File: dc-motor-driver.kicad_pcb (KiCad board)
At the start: 2 copper layers, 33 x 39.5 mm, 29 parts, among them J1 Conn_01x03, J10 Right, J11 RL, J12 RR, J2 MPU, J3 BAT, J4 Conn_01x03, J5 Power, J6 Left, J7 Conn_01x03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

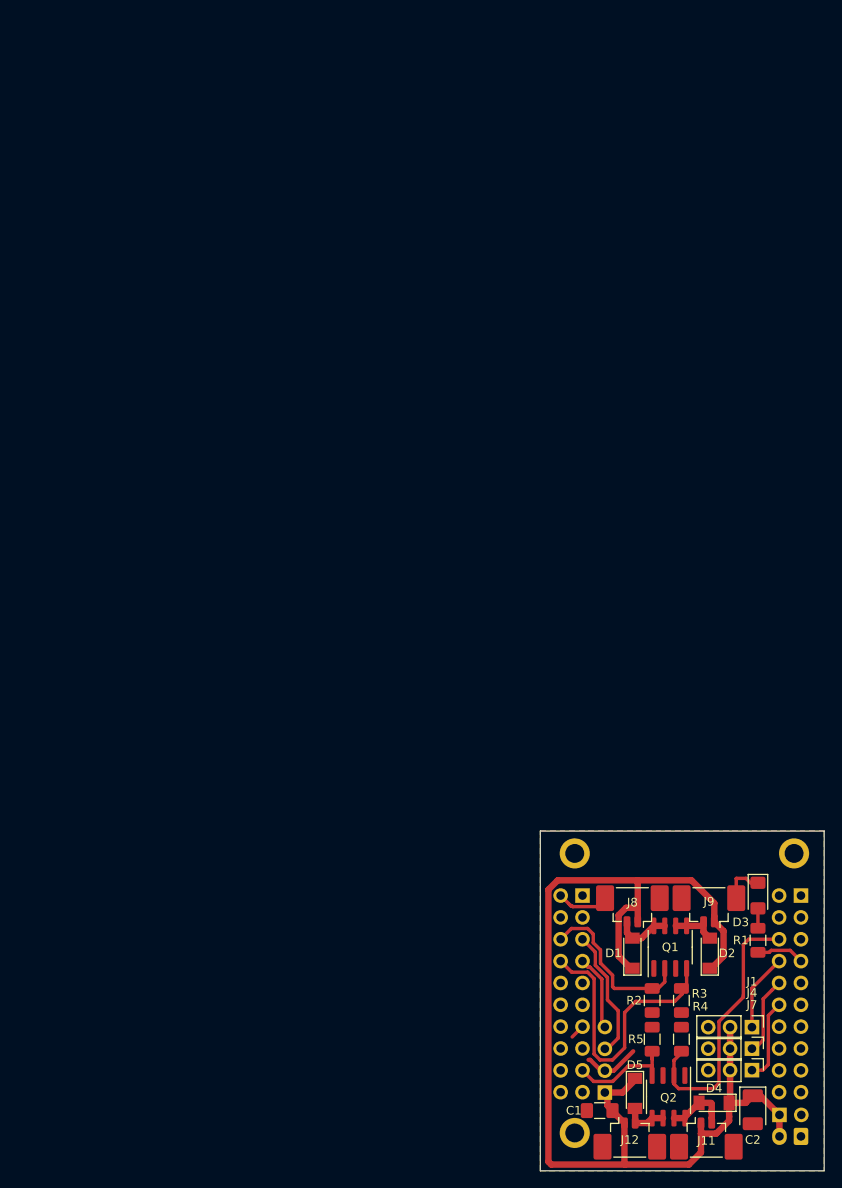
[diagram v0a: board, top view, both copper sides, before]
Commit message: Moved the PCB to a more convenient location.
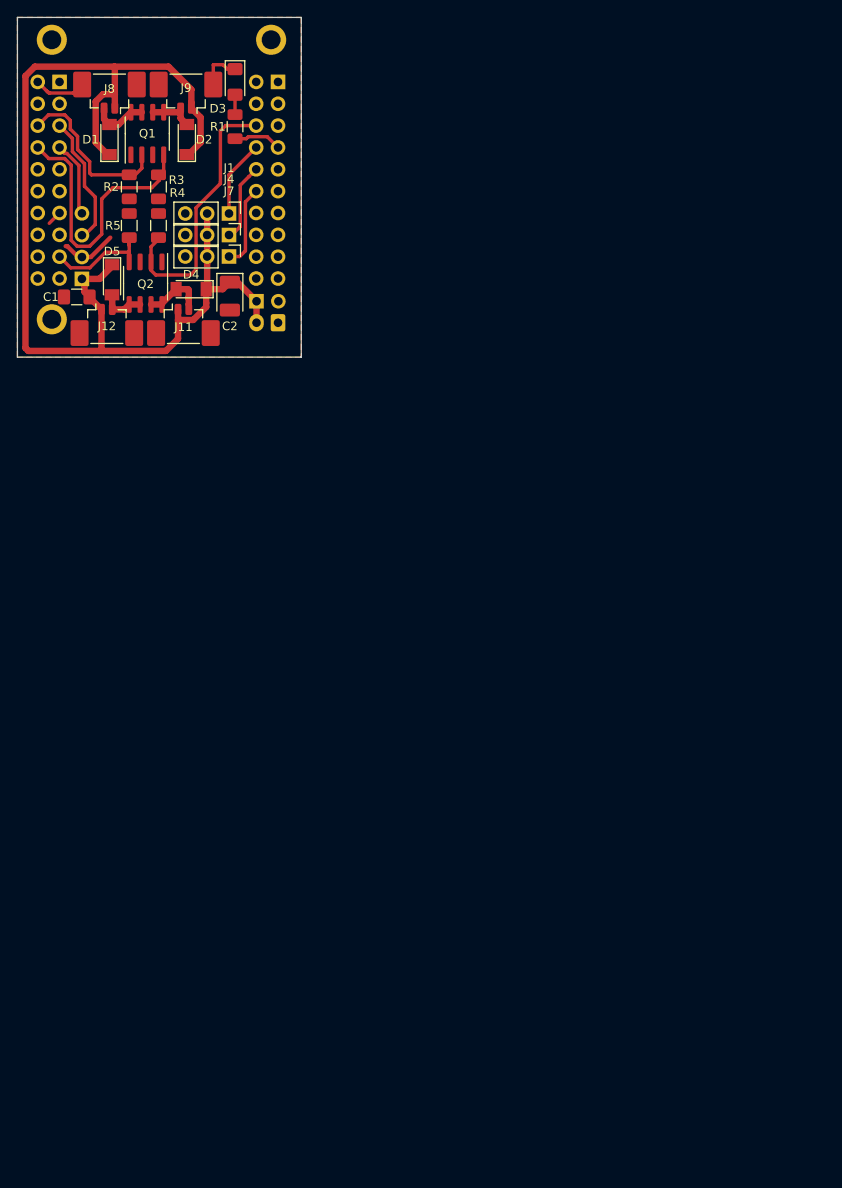
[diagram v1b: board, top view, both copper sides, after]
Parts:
- moved C2 112.5 mm to (42.9, 47.8)
- moved J1 112.5 mm to (42.8, 38.2)
- moved J2 112.5 mm to (25.7, 45.8)
- moved J4 112.5 mm to (42.8, 40.7)
- moved J7 112.5 mm to (42.8, 43.2)
- moved Q2 112.5 mm to (33.1, 46.3)
- moved ? 112.5 mm to (22.2, 18.0)
- moved ? 112.5 mm to (22.2, 50.5)
- moved ? 112.5 mm to (47.7, 18.0)
- moved C1 112.5 mm to (25.1, 47.9)
- moved D1 112.5 mm to (28.9, 29.6)
- moved D2 112.5 mm to (37.9, 29.6)
- moved D3 112.5 mm to (43.5, 22.9)
- moved D4 112.5 mm to (38.4, 47.0)
- moved D5 112.5 mm to (29.2, 45.9)
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
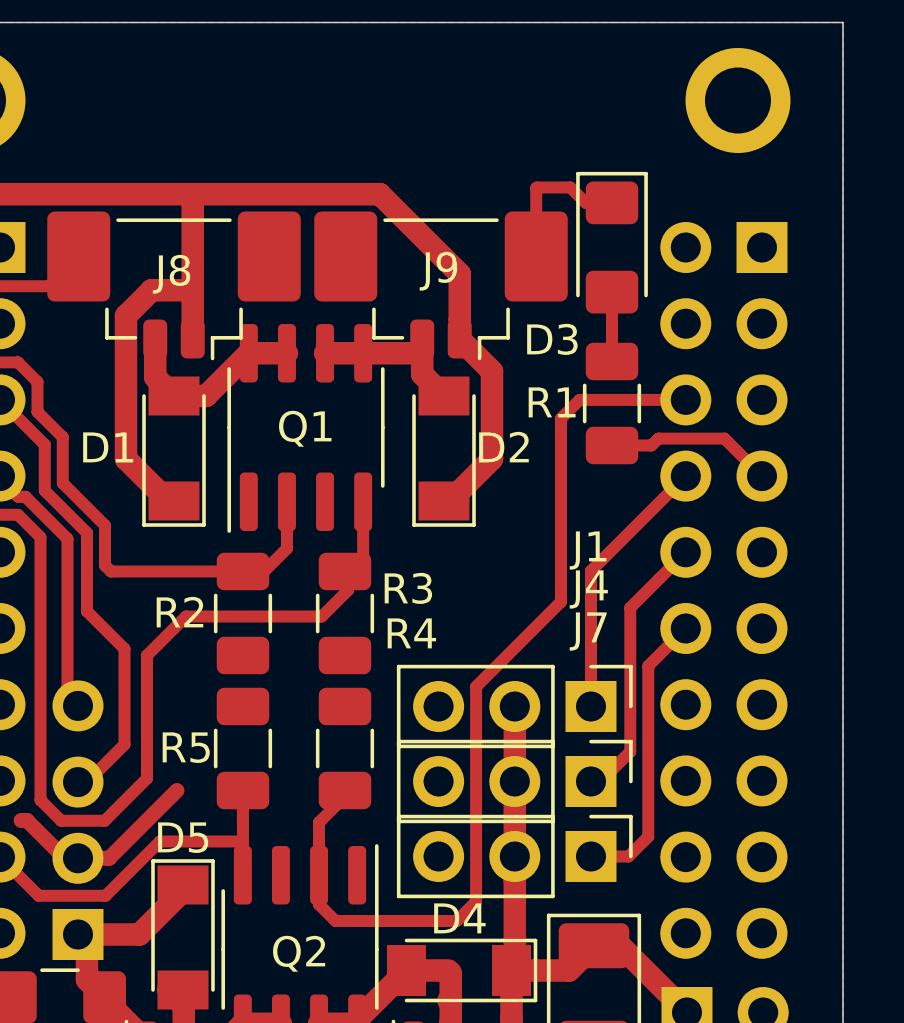
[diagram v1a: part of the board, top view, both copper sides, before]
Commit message: Moved servos & led pins to output-enabled pins.
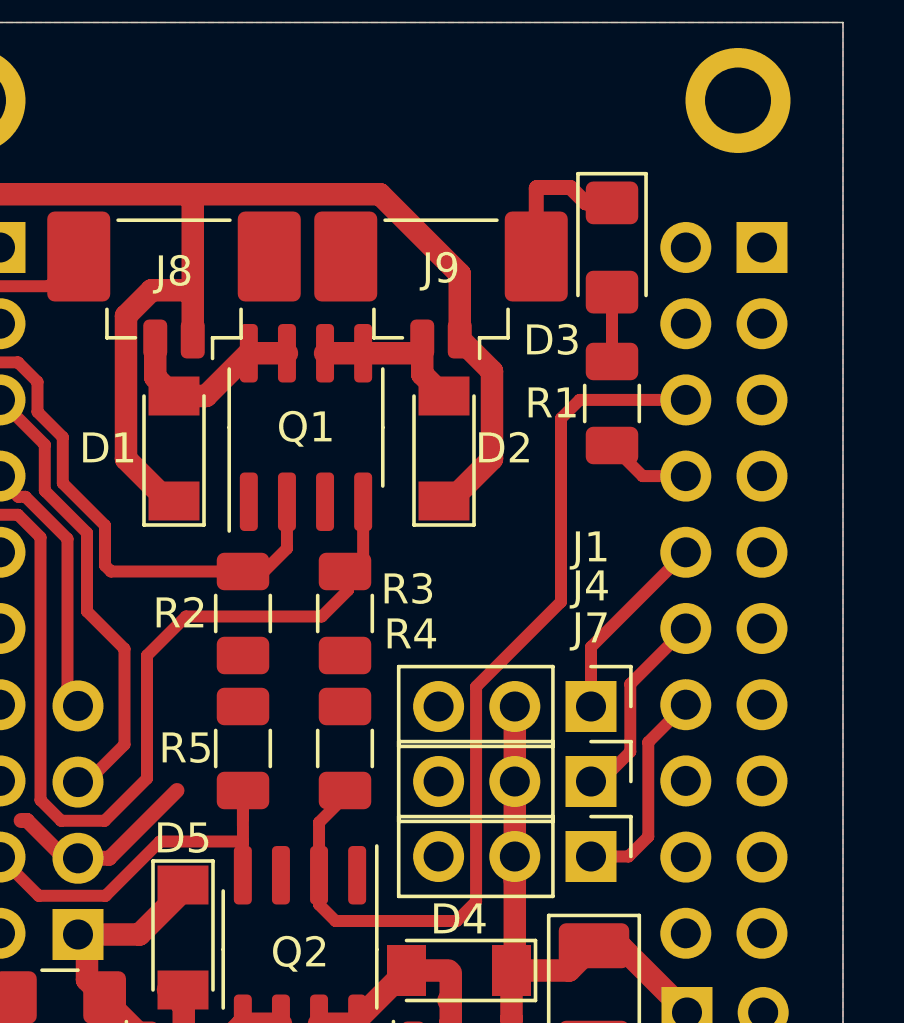
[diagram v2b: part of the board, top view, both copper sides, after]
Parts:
- R1: value 10k -> 1k
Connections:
- J11 pad MP: GND -> (no net)
- J12 pad MP: GND -> (no net)
- J6 pad 10: /ServoB -> /ServoA
- J6 pad 12: /ServoC -> /ServoB
- J6 pad 14: Net-(J6-Pad14) -> /ServoC
- J6 pad 7: /LED -> Net-(J6-Pad7)
- J6 pad 8: /ServoA -> /LED
- J8 pad MP: GND -> (no net)
- J9 pad MP: GND -> (no net)
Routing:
- net /ServoA: track 9.39 -> 6.45 mm
- net /ServoB: track 9.55 -> 7.01 mm
- net /ServoC: track 9.64 -> 7.10 mm
- net /LED: track 5.31 -> 2.88 mm
- net GND: track 19.5 -> 20.3 mm

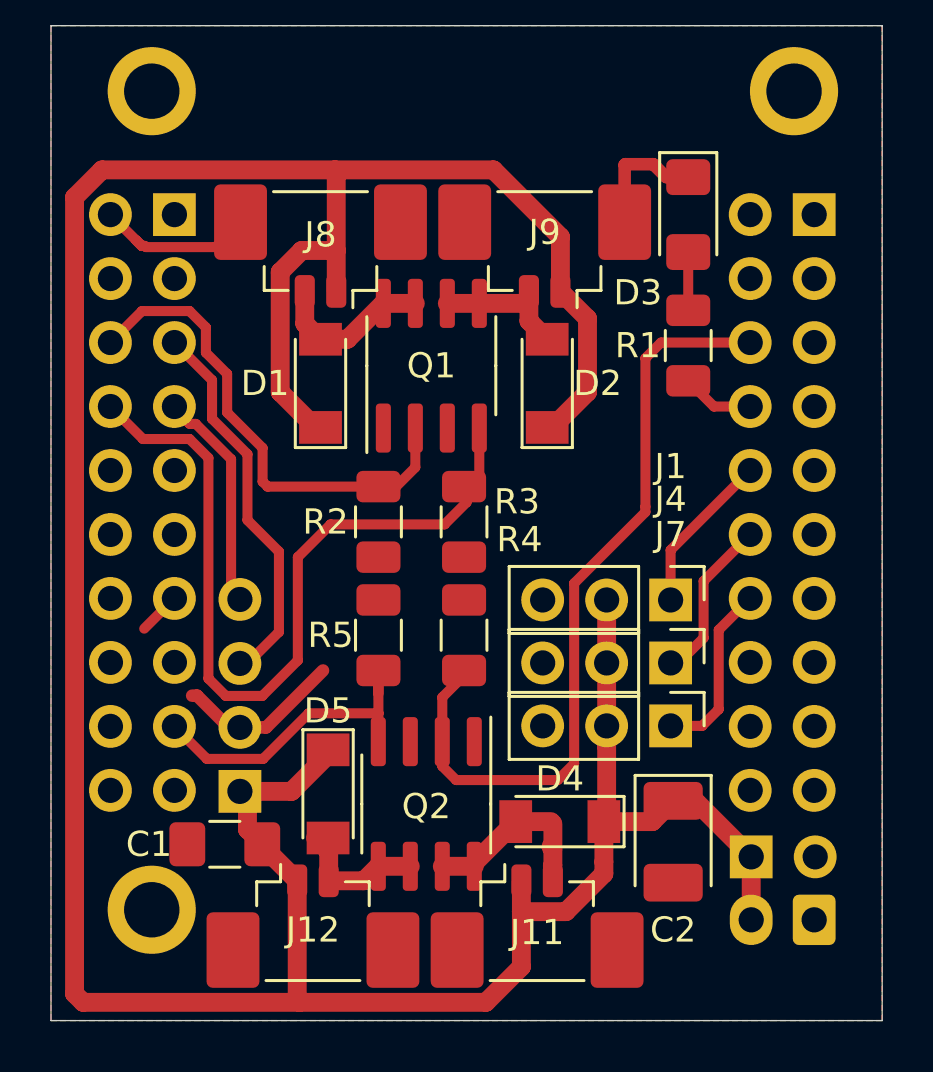
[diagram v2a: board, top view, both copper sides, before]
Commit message: Changed the power source for the MPU.
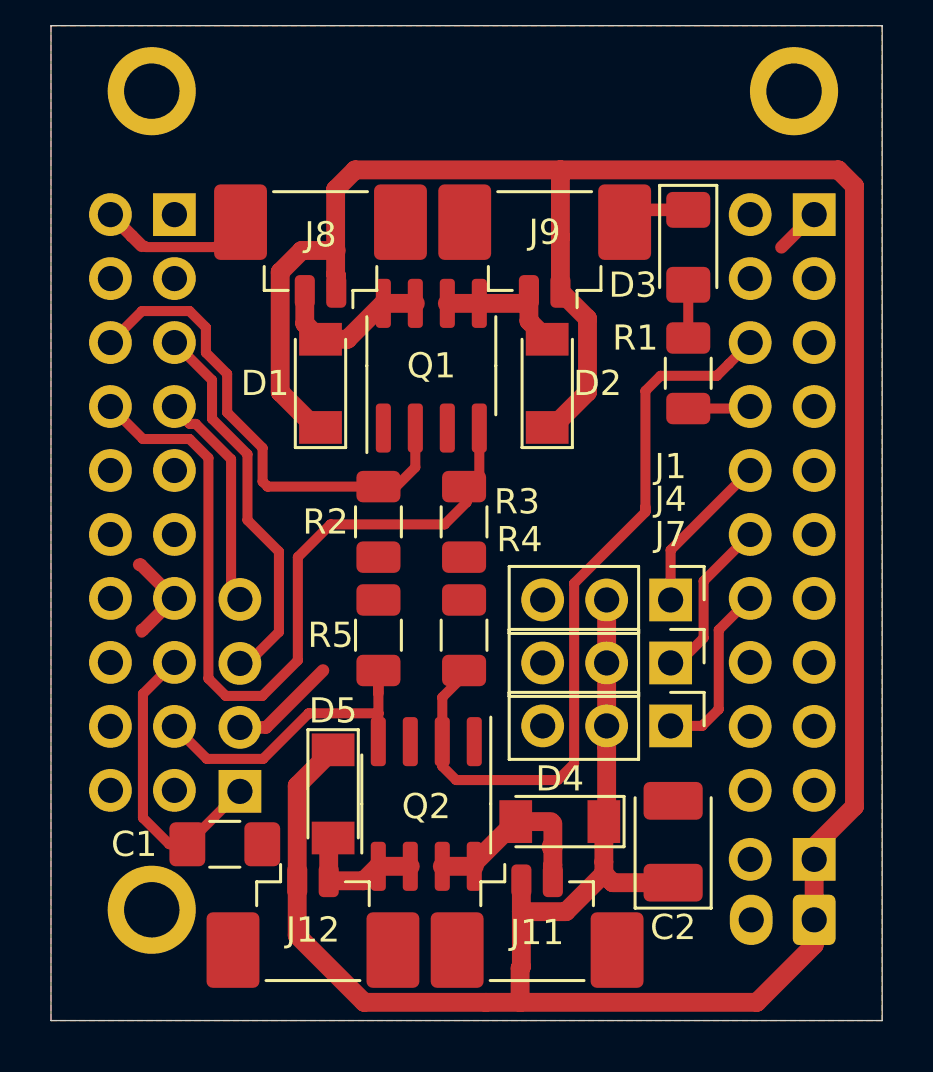
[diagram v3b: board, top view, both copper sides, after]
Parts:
- moved J5 2.50 mm to (48.5, 48.5), turned to 90 degrees
- moved D3 1.30 mm to (43.5, 24.2)
- moved R1 1.10 mm to (43.5, 29.2)
- moved D5 0.20 mm to (29.4, 45.9)
- turned C1 to 0 degrees
- turned C2 to 90 degrees
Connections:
- C1 pad 1: VCC -> +5V
- J10 pad 15: Net-(J10-Pad15) -> +5V
- J11 pad MP: (no net) -> GND
- J12 pad MP: (no net) -> GND
- J2 pad 1: VCC -> +5V
- J3 pad 1: GND -> VCC
- J3 pad 2: VCC -> GND
- J8 pad MP: (no net) -> GND
- J9 pad MP: (no net) -> GND
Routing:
- net +5V: track 0.00 -> 11.8 mm
- net VCC: track 135.3 -> 130.1 mm
- net GND: track 20.3 -> 21.2 mm
- net Net-(D5-Pad2): track 5.43 -> 4.69 mm
- net /RL: track 31.7 -> 31.1 mm
